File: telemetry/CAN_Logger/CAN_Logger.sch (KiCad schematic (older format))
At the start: 47 parts, among them J1 CONN_02X03, U1 MCP2561-E_SN, U101 TPS560430YF, U2 ATMEGA16M1, Y1 Crystal_SMD

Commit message: New Level Shifter, Changes from Feedback
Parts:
- removed U?: TXB0104, Housings_SSOP:TSSOP-14_4.4x5mm_Pitch0.65mm, symbol formula:TXB0104
- added U1: TXB0108, Package_SO:TSSOP-20_4.4x6.5mm_P0.65mm, symbol formula:TXB0108
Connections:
- no-connect marks 15 -> 23
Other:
- note added: "8-BIT 5V-3V3 LEVEL SHIFTER"
- note removed: "5V-3V3 LEVEL SHIFTER"
- moved on the sheet: C8, C9
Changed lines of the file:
@@
 Text Notes 1300 6150 0    50   ~ 0
 LINEAR VOLTAGE REGULATOR
-Text Notes 4750 6100 0    50   ~ 0
-5V-3V3 LEVEL SHIFTER
-$Comp
-L power:VCC #PWR?
-U 1 1 5FA5A02D
-P 6150 6400
-F 0 "#PWR?" H 6150 6250 50  0001 C CNN
-F 1 "VCC" H 6165 6573 50  0000 C CNN
-F 2 "" H 6150 6400 50  0001 C CNN
-F 3 "" H 6150 6400 50  0001 C CNN
-	1    6150 6400
-	1    0    0    -1
-$EndComp
-Wire Wire Line
-	4750 7100 4750 7250
+Text Notes 4700 5850 0    50   ~ 0
+8-BIT 5V-3V3 LEVEL SHIFTER
+Wire Wire Line
+	5700 7200 5700 7350
 $Comp
 L power:GND #PWR?
 U 1 1 5FA9384F
-P 4750 7250
-F 0 "#PWR?" H 4750 7000 50  0001 C CNN
-F 1 "GND" H 4755 7077 50  0000 C CNN
-F 2 "" H 4750 7250 50  0001 C CNN
-F 3 "" H 4750 7250 50  0001 C CNN
-	1    4750 7250
+P 5700 7350
+F 0 "#PWR?" H 5700 7100 50  0001 C CNN
+F 1 "GND" H 5705 7177 50  0000 C CNN
+F 2 "" H 5700 7350 50  0001 C CNN
+F 3 "" H 5700 7350 50  0001 C CNN
+	1    5700 7350
 	1    0    0    -1
 $EndComp
@@
 L power:+3.3V #PWR?
 U 1 1 5FA600D5
-P 4250 6400
-F 0 "#PWR?" H 4250 6250 50  0001 C CNN
-F 1 "+3.3V" H 4265 6573 50  0000 C CNN
-F 2 "" H 4250 6400 50  0001 C CNN
-F 3 "" H 4250 6400 50  0001 C CNN
-	1    4250 6400
+P 4300 6200
+F 0 "#PWR?" H 4300 6050 50  0001 C CNN
+F 1 "+3.3V" H 4315 6373 50  0000 C CNN
+F 2 "" H 4300 6200 50  0001 C CNN
+F 3 "" H 4300 6200 50  0001 C CNN
+	1    4300 6200
 	1    0    0    -1
 $EndComp
@@
 L formula:C_0.1uF C8
 U 1 1 5FA99092
-P 4250 6650
-F 0 "C8" H 4000 6700 50  0000 L CNN
-F 1 "C_0.1uF" H 3800 6600 50  0000 L CNN
-F 2 "footprints:C_0805_OEM" H 4288 6500 50  0001 C CNN
-F 3 "http://datasheets.avx.com/X7RDielectric.pdf" H 4275 6750 50  0001 C CNN
-F 4 "DK" H 4250 6650 60  0001 C CNN "MFN"
-F 5 "478-3352-1-ND" H 4250 6650 60  0001 C CNN "MPN"
-F 6 "https://www.digikey.com/products/en?keywords=478-3352-1-ND" H 4675 7150 60  0001 C CNN "PurchasingLink"
-	1    4250 6650
+P 4300 6450
+F 0 "C8" H 4050 6500 50  0000 L CNN
+F 1 "C_0.1uF" H 3850 6400 50  0000 L CNN
+F 2 "footprints:C_0805_OEM" H 4338 6300 50  0001 C CNN
+F 3 "http://datasheets.avx.com/X7RDielectric.pdf" H 4325 6550 50  0001 C CNN
+F 4 "DK" H 4300 6450 60  0001 C CNN "MFN"
+F 5 "478-3352-1-ND" H 4300 6450 60  0001 C CNN "MPN"
+F 6 "https://www.digikey.com/products/en?keywords=478-3352-1-ND" H 4725 6950 60  0001 C CNN "PurchasingLink"
+	1    4300 6450
 	1    0    0    -1
 $EndComp
@@
 	-1   0    0    1
 $EndComp
-$Comp
-L formula:TXB0104 U?
-U 1 1 5FA1ECD5
-P 5150 6350
-F 0 "U?" H 5200 6425 50  0000 C CNN
-F 1 "TXB0104" H 5200 6334 50  0000 C CNN
-F 2 "Housings_SSOP:TSSOP-14_4.4x5mm_Pitch0.65mm" H 5050 6250 50  0001 C CNN
-F 3 "http://www.ti.com/lit/ds/symlink/txb0104.pdf" H 5150 6350 50  0001 C CNN
-F 4 "DK" H 5250 6450 50  0001 C CNN "MFN"
-F 5 "296-21929-1-ND" H 5350 6550 50  0001 C CNN "MPN"
-F 6 "https://www.digikey.com/product-detail/en/texas-instruments/TXB0104PWR/296-21929-1-ND/1629282" H 5450 6650 50  0001 C CNN "PurchasingLink"
-	1    5150 6350
-	1    0    0    -1
-$EndComp
-$Comp
-L power:+3.3V #PWR?
-U 1 1 5FB3450C
-P 5900 7100
-F 0 "#PWR?" H 5900 6950 50  0001 C CNN
-F 1 "+3.3V" H 5915 7273 50  0000 C CNN
-F 2 "" H 5900 7100 50  0001 C CNN
-F 3 "" H 5900 7100 50  0001 C CNN
-	1    5900 7100
-	1    0    0    -1
-$EndComp
-Wire Wire Line
-	5650 7100 5900 7100
-Text Label 5650 6600 0    50   ~ 0
-MISO
-Text Label 5650 6700 0    50   ~ 0
-MOSI
-Text Label 5650 6800 0    50   ~ 0
-SCK
-Text Label 4750 6600 2    50   ~ 0
+Text Label 4800 6400 2    50   ~ 0
 MISO_3.3V
-Text Label 4750 6700 2    50   ~ 0
+Text Label 4800 6500 2    50   ~ 0
 MOSI_3.3V
-Text Label 4750 6800 2    50   ~ 0
+Text Label 4800 6600 2    50   ~ 0
 SCK_3.3V
 Text Label 7600 4050 2    50   ~ 0
@@
 Text Label 3650 3300 0    50   ~ 0
 CS
-Text Label 5650 6900 0    50   ~ 0
-CS
-Text Label 4750 6900 2    50   ~ 0
+Text Label 4800 6700 2    50   ~ 0
 CS_3.3V
 Text Label 7600 4350 2    50   ~ 0
@@
 Wire Wire Line
 	9100 2650 9150 2650
-$Comp
-L formula:C_0.1uF C9
-U 1 1 5FA9BD05
-P 6150 6650
-F 0 "C9" H 6265 6696 50  0000 L CNN
-F 1 "C_0.1uF" H 6265 6605 50  0000 L CNN
-F 2 "footprints:C_0805_OEM" H 6188 6500 50  0001 C CNN
-F 3 "http://datasheets.avx.com/X7RDielectric.pdf" H 6175 6750 50  0001 C CNN
-F 4 "DK" H 6150 6650 60  0001 C CNN "MFN"
-F 5 "478-3352-1-ND" H 6150 6650 60  0001 C CNN "MPN"
-F 6 "https://www.digikey.com/products/en?keywords=478-3352-1-ND" H 6575 7150 60  0001 C CNN "PurchasingLink"
-	1    6150 6650
-	1    0    0    -1
-$EndComp
-$Comp
-L power:GND #PWR?
-U 1 1 5FBA01E3
-P 6150 6900
-F 0 "#PWR?" H 6150 6650 50  0001 C CNN
-F 1 "GND" H 6155 6727 50  0000 C CNN
-F 2 "" H 6150 6900 50  0001 C CNN
-F 3 "" H 6150 6900 50  0001 C CNN
-	1    6150 6900
-	1    0    0    -1
-$EndComp
-Wire Wire Line
-	6150 6900 6150 6800
-Wire Wire Line
-	6150 6500 6150 6400
-Wire Wire Line
-	5650 6500 6150 6500
-Connection ~ 6150 6500
-Wire Wire Line
-	4250 6500 4250 6400
+Wire Wire Line
+	4300 6300 4300 6200
 $Comp
 L power:GND #PWR?
 U 1 1 5FBEF936
-P 4250 6900
-F 0 "#PWR?" H 4250 6650 50  0001 C CNN
-F 1 "GND" H 4255 6727 50  0000 C CNN
-F 2 "" H 4250 6900 50  0001 C CNN
-F 3 "" H 4250 6900 50  0001 C CNN
-	1    4250 6900
-	1    0    0    -1
-$EndComp
-Wire Wire Line
-	4250 6800 4250 6900
-Wire Wire Line
-	4250 6500 4750 6500
-Connection ~ 4250 6500
+P 4300 6700
+F 0 "#PWR?" H 4300 6450 50  0001 C CNN
+F 1 "GND" H 4305 6527 50  0000 C CNN
+F 2 "" H 4300 6700 50  0001 C CNN
+F 3 "" H 4300 6700 50  0001 C CNN
+	1    4300 6700
+	1    0    0    -1
+$EndComp
+Wire Wire Line
+	4300 6600 4300 6700
+Wire Wire Line
+	4300 6300 4800 6300
+Connection ~ 4300 6300
 $Comp
 L formula:SD_socket J?
@@
 NoConn ~ 3650 3400
 NoConn ~ 3650 3500
+NoConn ~ 4800 7100
+NoConn ~ 4800 7000
+NoConn ~ 4800 6900
+NoConn ~ 4800 6800
+$Comp
+L formula:TXB0108 U1
+U 1 1 5FC3D37A
+P 5250 6250
+F 0 "U1" H 5250 6425 50  0000 C CNN
+F 1 "TXB0108" H 5250 6334 50  0000 C CNN
+F 2 "Package_SO:TSSOP-20_4.4x6.5mm_P0.65mm" H 5150 6700 50  0001 C CNN
+F 3 "https://www.ti.com/lit/ds/symlink/txb0108.pdf?HQS=TI-null-null-digikeymode-df-pf-null-wwe&ts=1605211774233" H 5200 6350 50  0001 C CNN
+F 4 "DK" H 5250 6400 50  0001 C CNN "MFN"
+F 5 "296-21527-1-ND" H 5350 6500 50  0001 C CNN "MPN"
+F 6 "https://www.digikey.com/en/products/detail/texas-instruments/TXB0108PWR/1305699" H 5450 6600 50  0001 C CNN "PurchasingLink"
+	1    5250 6250
+	1    0    0    -1
+$EndComp
+Connection ~ 6200 6300
+Wire Wire Line
+	5700 6300 6200 6300
+Wire Wire Line
+	6200 6300 6200 6200
+Wire Wire Line
+	6200 6700 6200 6600
+$Comp
+L power:GND #PWR?
+U 1 1 5FBA01E3
+P 6200 6700
+F 0 "#PWR?" H 6200 6450 50  0001 C CNN
+F 1 "GND" H 6205 6527 50  0000 C CNN
+F 2 "" H 6200 6700 50  0001 C CNN
+F 3 "" H 6200 6700 50  0001 C CNN
+	1    6200 6700
+	1    0    0    -1
+$EndComp
+$Comp
+L formula:C_0.1uF C9
+U 1 1 5FA9BD05
+P 6200 6450
+F 0 "C9" H 6315 6496 50  0000 L CNN
+F 1 "C_0.1uF" H 6315 6405 50  0000 L CNN
+F 2 "footprints:C_0805_OEM" H 6238 6300 50  0001 C CNN
+F 3 "http://datasheets.avx.com/X7RDielectric.pdf" H 6225 6550 50  0001 C CNN
+F 4 "DK" H 6200 6450 60  0001 C CNN "MFN"
+F 5 "478-3352-1-ND" H 6200 6450 60  0001 C CNN "MPN"
+F 6 "https://www.digikey.com/products/en?keywords=478-3352-1-ND" H 6625 6950 60  0001 C CNN "PurchasingLink"
+	1    6200 6450
+	1    0    0    -1
+$EndComp
+Text Label 5700 6700 0    50   ~ 0
+CS
+Text Label 5700 6600 0    50   ~ 0
+SCK
+Text Label 5700 6500 0    50   ~ 0
+MOSI
+Text Label 5700 6400 0    50   ~ 0
+MISO
+Wire Wire Line
+	4800 7200 4550 7200
+$Comp
+L power:+3.3V #PWR?
+U 1 1 5FB3450C
+P 4550 7200
+F 0 "#PWR?" H 4550 7050 50  0001 C CNN
+F 1 "+3.3V" H 4565 7373 50  0000 C CNN
+F 2 "" H 4550 7200 50  0001 C CNN
+F 3 "" H 4550 7200 50  0001 C CNN
+	1    4550 7200
+	1    0    0    -1
+$EndComp
+$Comp
+L power:VCC #PWR?
+U 1 1 5FA5A02D
+P 6200 6200
+F 0 "#PWR?" H 6200 6050 50  0001 C CNN
+F 1 "VCC" H 6215 6373 50  0000 C CNN
+F 2 "" H 6200 6200 50  0001 C CNN
+F 3 "" H 6200 6200 50  0001 C CNN
+	1    6200 6200
+	1    0    0    -1
+$EndComp
+NoConn ~ 5700 6800
+NoConn ~ 5700 6900
+NoConn ~ 5700 7000
+NoConn ~ 5700 7100
 $EndSCHEMATC

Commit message: Fixed Annotations
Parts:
- gave numbers to parts that had none: 2
- renumbered U1 to U4

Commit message: Design Checklist, Edit Resistors
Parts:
- added U5, U6, U7: R_500, symbol formula:R_500
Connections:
- net labels added: +5V, MISO_SD, MOSI_SD, SCK_SD
- net labels removed: 5V, VCC
- wire segments 105 -> 109
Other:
- note removed: "5V"
- moved on the sheet: R5, R6

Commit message: Removed and replaced rescue
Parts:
- C1, C101, C103, C2: symbol template-rescue:C_0.1uF-formula -> formula:C_0.1uF
- C102: footprint footprints:C_0603_1608Metric -> footprints:C_0805_OEM; symbol template-rescue:C_2.2uF-formula -> formula:C_2.2uF; MFN DK -> (none); MPN 311-1451-1-ND -> (none); PurchasingLink https://www.digikey.com/product-detail/en/yageo/CC0603KRX5R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 -> https://www.digikey.com/product-detail/en/tdk-corporation/C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
- C3: symbol template-rescue:C_100pF-formula -> formula:C_100pF
- C4, C5: symbol template-rescue:C_30pF-formula -> formula:C_30pF
- COUT101: symbol template-rescue:C_22uF-formula -> formula:C_22uF
- COUT102: symbol template-rescue:C_33uF-formula -> formula:C_33uF; MFN C4532X7R1C336M250KC -> DK
- COUT103: symbol template-rescue:C_47uF-formula -> formula:C_47uF
- D101: symbol template-rescue:D_Zener_18V-formula -> formula:D_Zener_18V
- D102, D103: symbol template-rescue:LED_0805-formula -> formula:LED_0805
- F101: symbol template-rescue:F_500mA_16V-formula -> formula:F_500mA_16V
- J1: symbol template-rescue:CONN_02X03-formula -> formula:CONN_02X03
- L101: footprint formula:L_100uH -> footprints:L_100uH_OEM; symbol template-rescue:L_100uH-formula -> formula:L_100uH; Link https://www.digikey.com/product-detail/en/tdk-corporation/N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 -> (none); MFN Digikey -> DK; PurchasingLink (none) -> https://www.digikey.com/product-detail/en/tdk-corporation/N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
- R102: symbol template-rescue:R_25K-formula -> formula:R_25K; Digi-key Part Number CPF-A-0805B25KE -> (none); MFN A124124CT-ND -> DK; MPN (none) -> A124124CT-ND
- R103: symbol template-rescue:R_100K-formula -> formula:R_100K
- R104: symbol template-rescue:R_0_2512-formula -> formula:R_0_2512
- R105: symbol template-rescue:R_200-formula -> formula:R_200
- R7: symbol template-rescue:R_10K-formula -> formula:R_10K
- R8: symbol template-rescue:R_100-formula -> formula:R_100
- U1: symbol template-rescue:MCP2561-E_SN-formula -> formula:MCP2561-E_SN
- U101: symbol template-rescue:TPS560430YF-formula -> formula:TPS560430YF; MFN TPS560430YFDBVR-ND -> DK; MPN TPS560430YFDBVR -> TPS560430YFDBVR-ND; Purchasing Link https://www.digikey.com/product-detail/en/texas-instruments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 -> (none); PurchasingLink (none) -> https://www.digikey.com/product-detail/en/texas-instruments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
- U2: symbol template-rescue:ATMEGA16M1-formula -> formula:ATMEGA16M1
- Y1: symbol template-rescue:Crystal_SMD-formula -> formula:Crystal_SMD
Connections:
- net +5V: no longer C1.1, R8.1
- net GND: no longer C102.2
- net at D101.1 (K), F101.1, R101.1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: no longer C101.1, C102.1
- net at L101.2, R103.1, R104.1: no longer COUT101.1, COUT102.1, COUT103.1
- net CAN_HI renamed CAN_P
- net CAN_LO renamed CAN_N
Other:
- moved on the sheet: C102

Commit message: Completed PCB Design Checklist, waiting on connector
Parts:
- removed U4: TXB0108, Package_SO:TSSOP-20_4.4x6.5mm_P0.65mm, symbol formula:TXB0108
- added TP1, TP2, TP3: Test_Point_SMD, footprints:Test_Point_SMD, symbol formula:Test_Point_SMD
- added U4: TXB0104, Package_SO:TSSOP-14_4.4x5mm_P0.65mm, symbol formula:TXB0104
- U3: footprint footprints:SOT-23-3_OEM -> Package_TO_SOT_SMD:SOT-23
- U5, U6, U7: footprint (none) -> footprints:R_0805_OEM
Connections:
- net +3V3: now also U4.1 (VCCA), U4.8 (OE)
- net +5V: now also C1.1, R8.1, TP1.1, U4.14 (VCCB)
- net 12V: now also TP2.1
- net CS: now also U4.10 (B4)
- net CS_3.3V: now also U4.5 (A4)
- net GND: now also C102.2, TP3.1, U4.7 (GND)
- net MISO_3.3V: now also U4.2 (A1)
- net MISO_SD: now also U4.13 (B1)
- net MOSI_3.3V: now also U4.3 (A2)
- net MOSI_SD: now also U4.12 (B2)
- net SCK_3.3V: now also U4.4 (A3)
- net SCK_SD: now also U4.11 (B3)
- net at C102.1: now also C101.1, D101.1 (K), F101.1, R101.1, U101.4 (EN), U101.5 (VIN)
- net at L101.2, R103.1, R104.1: now also COUT101.1, COUT102.1, COUT103.1
- no-connect marks 23 -> 15
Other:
- note added: "4-BIT 5V-3V3 LEVEL SHIFTER"
- note removed: "8-BIT 5V-3V3 LEVEL SHIFTER"
- moved on the sheet: C101, C102, C103, C6, C7, C8, C9, COUT101, COUT102, COUT103, D101, D102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

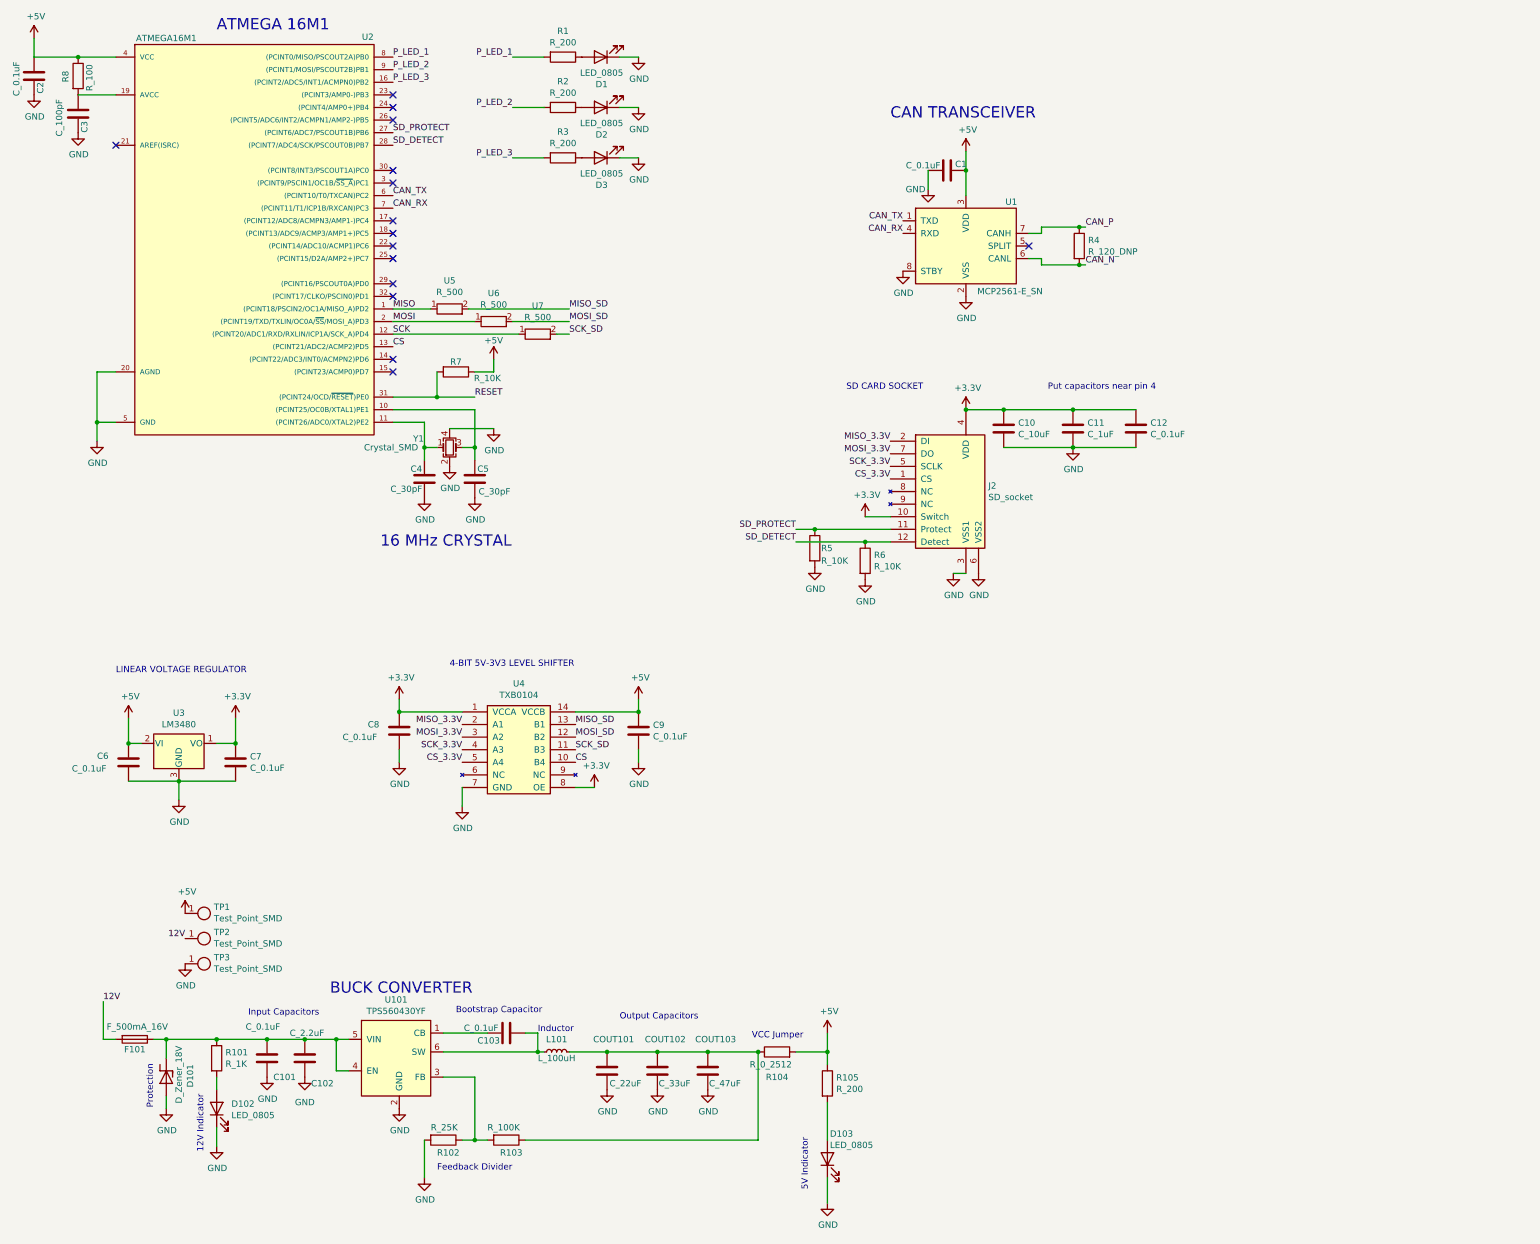
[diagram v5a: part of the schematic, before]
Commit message: Began PCB layout, and schematic layout boxing
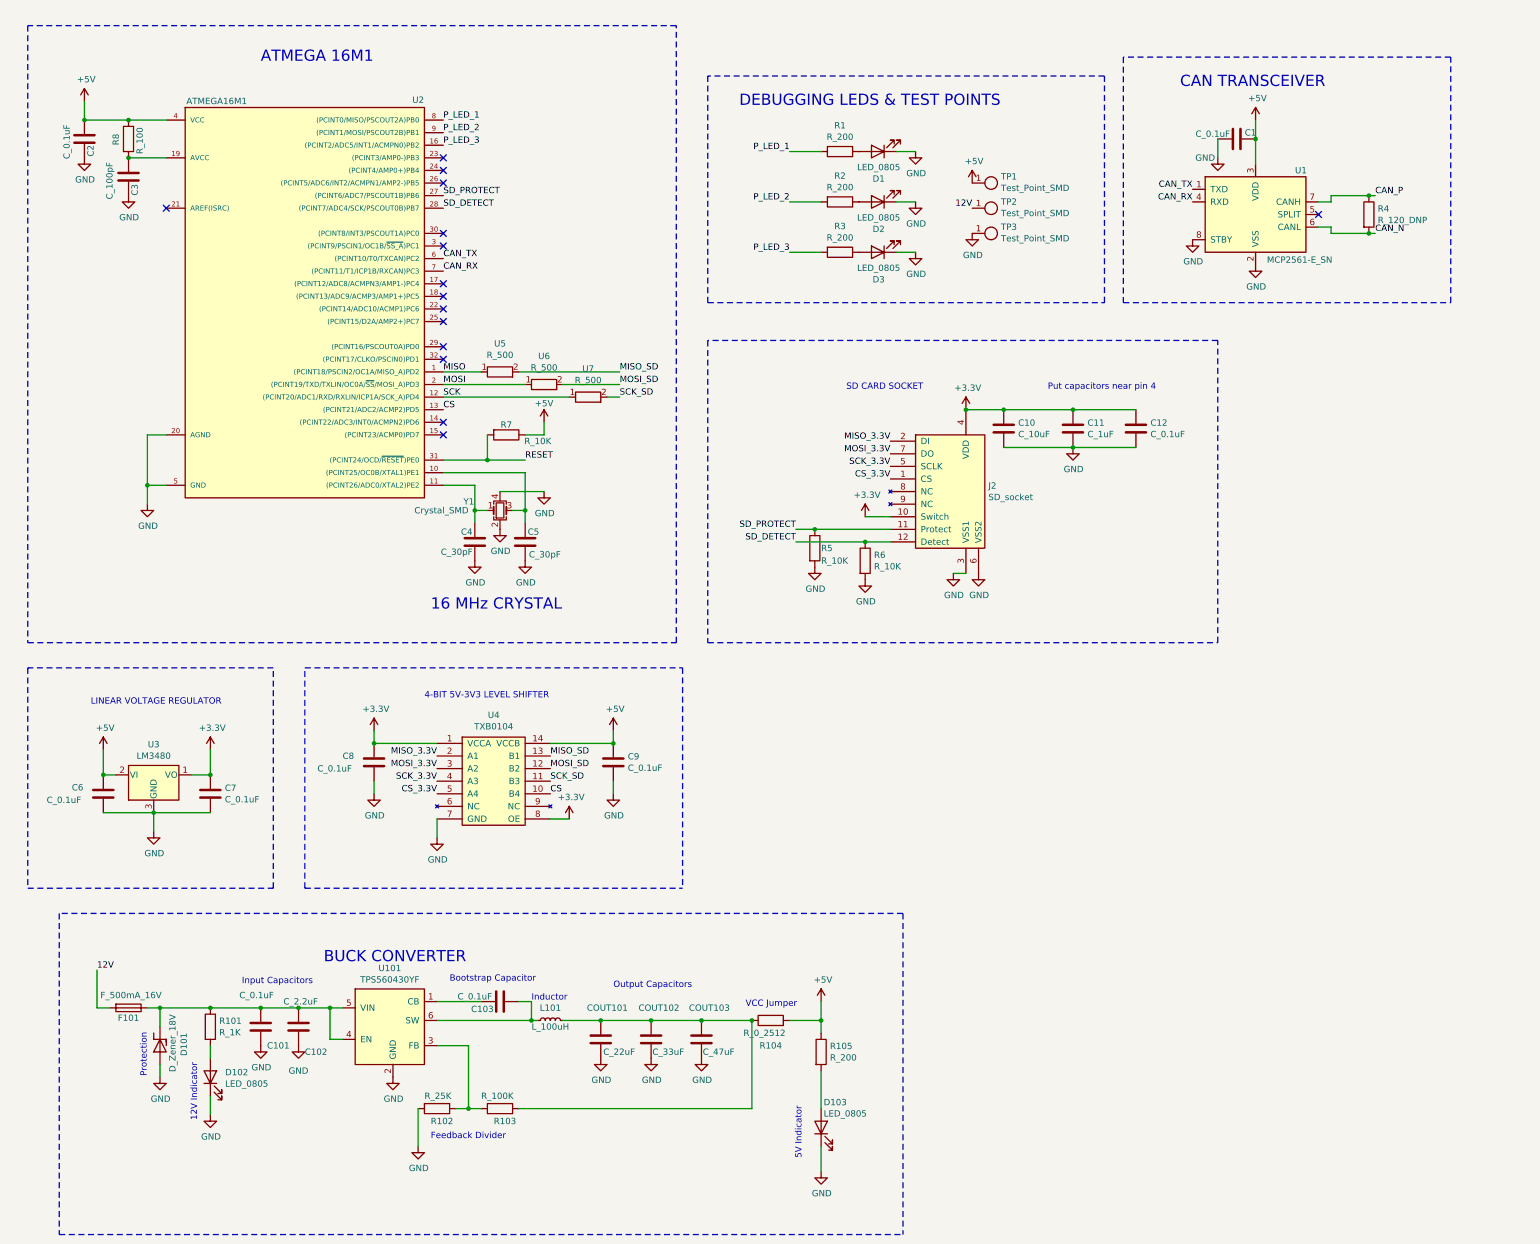
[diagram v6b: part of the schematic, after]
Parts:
- C102: footprint footprints:C_0805_OEM -> footprints:C_0603_1608Metric
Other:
- note added: "DEBUGGING LEDS & TEST POINTS"
- moved on the sheet: C1, C101, C102, C103, C2, C3, C4, C5, C6, C7, C8, C9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
